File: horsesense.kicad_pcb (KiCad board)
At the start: 4 copper layers, 30 x 60 mm, 65 parts, among them J1 USB4105-GF-A-120, J2 S2B-PH-SM4-TB, J3 73412-0110, J4 Conn_01x04, SW1 EVQ-P7A01P, SW2 EVQ-P7A01P, U1 MAX86141ENP+T, U2 TXB0304RUT, U3 BQ25601, U4 XC6210B332MR, U5 XC6210B182MR, U6 LC76GPAMD, U7 AP22804AW5, U9 ESP32-S3-WROOM-1-N16R8

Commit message: Set MPN
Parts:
- D1, D2, D3: value CT DBLP31.12-5C8C-56-J6Q6 -> CT DBLP31.12-6C5D-56-J6U6-20-R18
- L1: footprint Inductor_SMD:L_2010_5025Metric -> Inductor_SMD:L_0805_2012Metric
- R7: value R -> 0
- U2: value TXB0304RUT -> TXB0304RUTR
- U7: value AP22804AW5 -> AP22804AW5-7
- moved C14 2.81 mm to (145.1, 138.1), turned to 90 degrees
- moved L1 1.37 mm to (149.1, 137.7)
- moved C11 0.98 mm to (146.8, 142.6)
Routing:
- net Vsys: track 54.7 -> 57.8 mm, vias 6 -> 4
- net GND: track 73.1 -> 72.1 mm, vias 44 -> 43

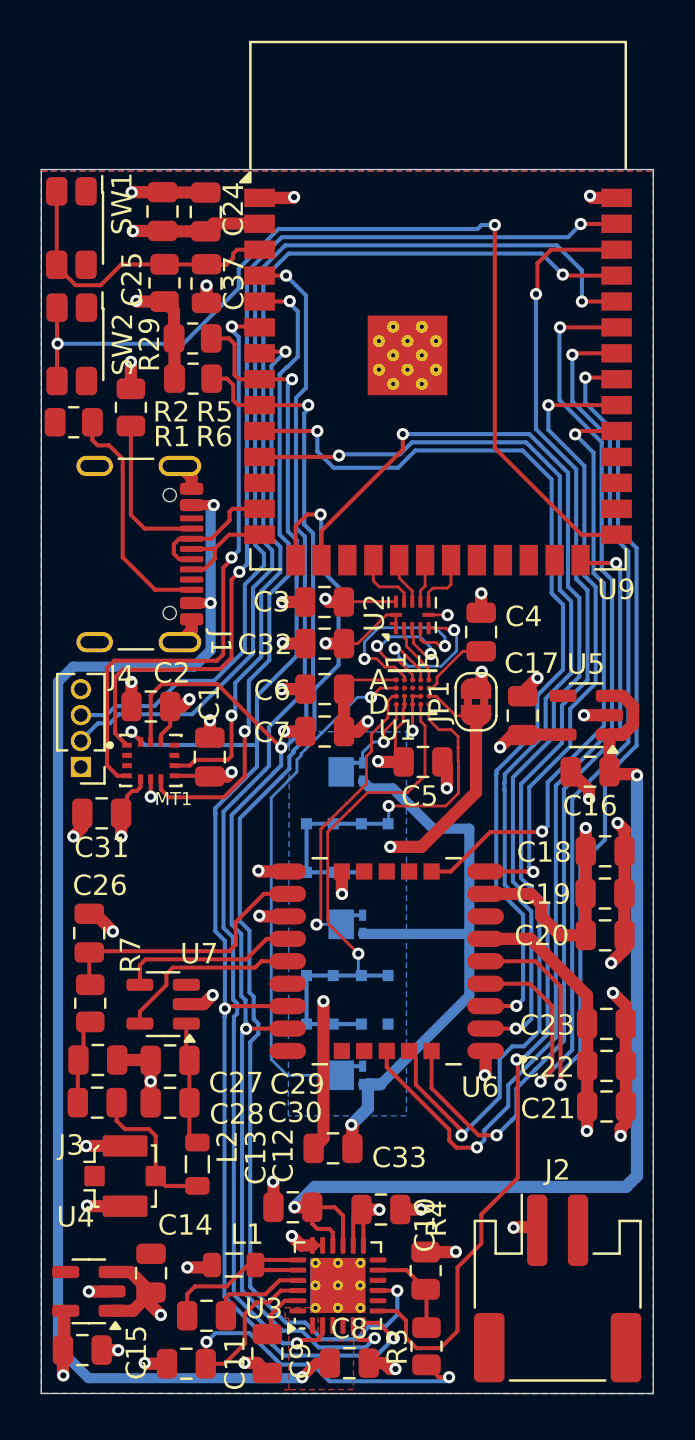
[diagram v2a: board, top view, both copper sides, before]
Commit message: Add Flash device
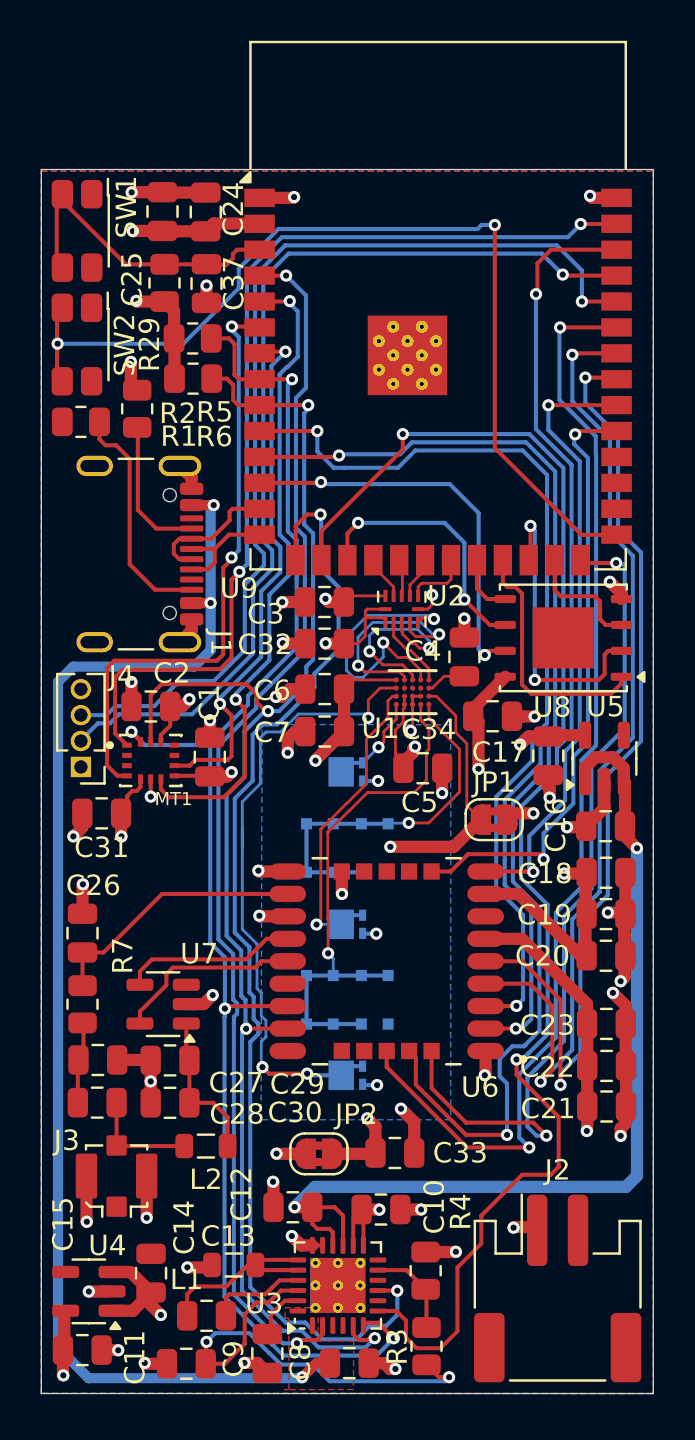
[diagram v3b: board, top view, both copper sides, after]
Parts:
- added C34: 100n, Capacitor_SMD:C_0805_2012Metric, F.Cu at (161.8, 110.8)
- added JP2: SolderJumper_2_Bridged, Jumper:SolderJumper-2_P1.3mm_Bridged2Bar_RoundedPad1.0x1.5mm, F.Cu at (153.3, 132.3)
- added U8: MX25L3233FM2, Package_DFN_QFN:W-PDFN-8-1EP_6x5mm_P1.27mm_EP3x3mm, F.Cu at (165.3, 107.0)
- moved JP1 5.85 mm to (161.9, 115.9), turned to 0 degrees
- moved C33 3.04 mm to (157.0, 132.2), turned to 0 degrees
- moved C16 2.78 mm to (167.3, 116.2)
- moved C17 2.33 mm to (164.5, 112.8), turned to -90 degrees
- moved U5 2.30 mm to (167.3, 112.9), turned to 90 degrees
- moved C4 1.47 mm to (160.4, 107.9)
- moved C18 1.05 mm to (167.4, 118.5)
- moved C19 1.01 mm to (167.4, 120.5)
- moved C20 1.00 mm to (167.4, 122.6)
- moved L2 0.98 mm to (147.8, 131.9), turned to 0 degrees
- moved U2 0.59 mm to (157.4, 105.6)
- moved J3 0.42 mm to (143.4, 133.4), turned to 180 degrees
- moved R7 0.38 mm to (141.7, 124.9)
- moved R1 0.35 mm to (141.6, 96.4)
- moved C26 0.33 mm to (141.7, 121.5)
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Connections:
- C33 pad 1: +3.3V -> +3.3V_LED
- D1 pad 2: +3.3V -> +3.3V_LED
- D2 pad 2: +3.3V -> +3.3V_LED
- D3 pad 2: +3.3V -> +3.3V_LED
- U9 pad 12: unconnected-(U9-IO8-Pad12) -> FLASH_SID3
- U9 pad 17: unconnected-(U9-IO9-Pad17) -> FLASH_SCLK
- U9 pad 22: unconnected-(U9-IO14-Pad22) -> FLASH_SID0
- U9 pad 23: unconnected-(U9-IO21-Pad23) -> FLASH_CS
- U9 pad 24: unconnected-(U9-IO47-Pad24) -> FLASH_SID1
- U9 pad 25: unconnected-(U9-IO48-Pad25) -> FLASH_SID2
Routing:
- net +3.3V: track 88.5 -> 64.5 mm, vias 11 -> 12
- net FLASH_SID3: track 0.00 -> 19.6 mm, vias 0 -> 2
- net FLASH_SID1: track 0.00 -> 14.9 mm, vias 0 -> 2
- net FLASH_SCLK: track 0.00 -> 13.0 mm, vias 0 -> 2
- net FLASH_CS: track 0.00 -> 12.5 mm
- net +3.3V_LED: track 0.00 -> 6.16 mm, vias 0 -> 4
- net FLASH_SID2: track 0.00 -> 5.98 mm
- net Net-(D3-K): track 26.6 -> 31.7 mm, vias 1 -> 3
- net MAX_MOSI_1_8: track 8.41 -> 13.3 mm
- net PD_GND: track 19.3 -> 14.7 mm
- net GND: track 72.1 -> 76.4 mm, vias 43 -> 44
- net Vsys: track 57.8 -> 54.5 mm
- net FLASH_SID0: track 0.00 -> 2.99 mm
- net GPS_FIX: track 38.5 -> 41.3 mm
- net SDA: track 75.0 -> 72.7 mm
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- added copper zone on In2.Cu, net +3.3V_LED

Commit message: Add mire and sizing marks
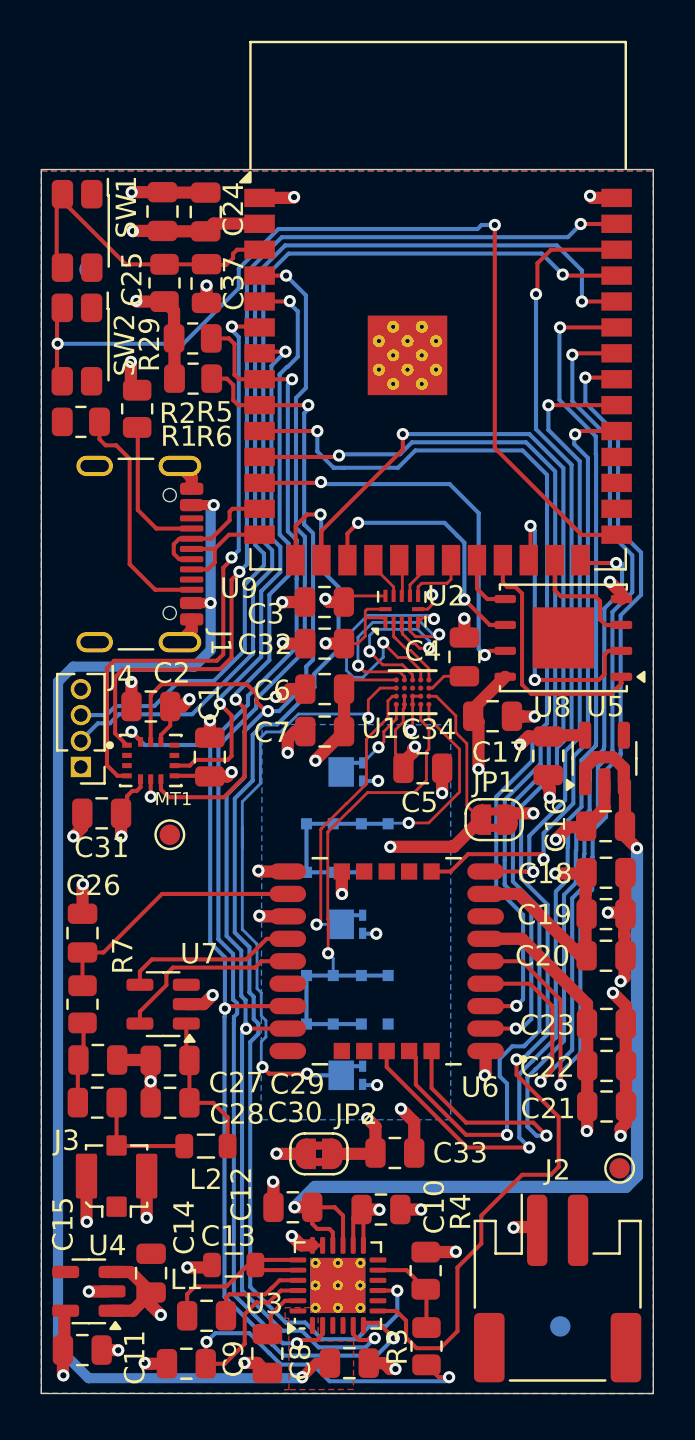
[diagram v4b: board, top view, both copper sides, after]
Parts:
- added TP1: Mire1_Top, TestPoint:TestPoint_Pad_D1.0mm, F.Cu at (146.0, 116.6)
- added TP2: Mire2_Top, TestPoint:TestPoint_Pad_D1.0mm, F.Cu at (168.0, 133.0)
- added TP3: Mire1_Bot, TestPoint:TestPoint_Pad_D1.0mm, B.Cu at (165.1, 140.7)
- added TP4: Mire2_Bot, TestPoint:TestPoint_Pad_D1.0mm, B.Cu at (142.1, 88.9)
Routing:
- net GND: track 76.4 -> 77.2 mm

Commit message: Ass logo
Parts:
- added SYM1: https://github.com/Philippe12/HorseSense, Symbol:OSHW-Symbol_13.4x12mm_SilkScreen, B.Cu at (158.7, 92.8)
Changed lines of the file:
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@@
+		(embedded_fonts no)
+	)
+	(footprint "Symbol:OSHW-Symbol_13.4x12mm_SilkScreen"
+		(layer "B.Cu")
+		(at 158.71 92.81 -90)
+		(descr "Open Source Hardware Symbol")
+		(tags "Logo Symbol OSHW")
+		(property "Reference" "SYM1"
+			(at 0 0 90)
+			(layer "B.SilkS")
+			(hide yes)
+			(effects
+				(font
+					(size 1 1)
+					(thickness 0.15)
+				)
+				(justify mirror)
+			)
+		)
+		(property "Value" "https://github.com/Philippe12/HorseSense"
+			(at 9.82 -8.79 90)
+			(layer "B.SilkS")
+			(effects
+				(font
+					(size 1 1)
+					(thickness 0.15)
+				)
+				(justify mirror)
+			)
+		)
+		(property "Datasheet" "~"
+			(at 0 0 90)
+			(unlocked yes)
+			(layer "B.Fab")
+			(hide yes)
+			(effects
+				(font
+					(size 1.27 1.27)
+					(thickness 0.15)
+				)
+				(justify mirror)
+			)
+		)
+		(property "Description" "Open Hardware logo, large"
+			(at 0 0 90)
+			(unlocked yes)
+			(layer "B.Fab")
+			(hide yes)
+			(effects
+				(font
+					(size 1.27 1.27)
+					(thickness 0.15)
+				)
+				(justify mirror)
+			)
+		)
+		(property "Sim.Enable" "0"
+			(at 0 0 90)
+			(unlocked yes)
+			(layer "B.Fab")
+			(hide yes)
+			(effects
+				(font
+					(size 1 1)
+					(thickness 0.15)
+				)
+				(justify mirror)
+			)
+		)
+		(sheetname "/")
+		(sheetfile "horsesense.kicad_sch")
+		(attr exclude_from_pos_files exclude_from_bom allow_missing_courtyard)
+		(fp_poly
+			(pts
+				(xy 1.119803 5.09936) (xy 1.288676 4.203573) (xy 1.911796 3.946702) (xy 2.534916 3.689832) (xy 3.282453 4.198151)
+				(xy 3.491802 4.339684) (xy 3.681043 4.466055) (xy 3.841343 4.571493) (xy 3.963874 4.65023) (xy 4.039802 4.696495)
+				(xy 4.06048 4.706471) (xy 4.097731 4.680814) (xy 4.177332 4.609885) (xy 4.290361 4.502743) (xy 4.427895 4.36845)
+				(xy 4.581012 4.216066) (xy 4.740789 4.054653) (xy 4.898305 3.89327) (xy 5.044637 3.740978) (xy 5.170863 3.606838)
+				(xy 5.26806 3.499911) (xy 5.327307 3.429258) (xy 5.341471 3.405612) (xy 5.321087 3.362021) (xy 5.263941 3.266519)
+				(xy 5.176041 3.12845) (xy 5.063396 2.957155) (xy 4.932013 2.761975) (xy 4.855882 2.650648) (xy 4.717118 2.447367)
+				(xy 4.593811 2.263927) (xy 4.491945 2.109458) (xy 4.417501 1.993091) (xy 4.376461 1.923958) (xy 4.370294 1.90943)
+				(xy 4.384274 1.86814) (xy 4.422382 1.771908) (xy 4.478867 1.634266) (xy 4.54798 1.468742) (xy 4.62397 1.288868)
+				(xy 4.701089 1.108172) (xy 4.773585 0.940186) (xy 4.835709 0.79844) (xy 4.881712 0.696463) (xy 4.905843 0.647786)
+				(xy 4.907267 0.64587) (xy 4.945158 0.636575) (xy 5.046069 0.61584) (xy 5.19954 0.585702) (xy 5.395112 0.548199)
+				(xy 5.622325 0.505371) (xy 5.754891 0.480674) (xy 5.997679 0.434447) (xy 6.216974 0.39046) (xy 6.401681 0.351119)
+				(xy 6.540705 0.318831) (xy 6.622952 0.296003) (xy 6.639485 0.28876) (xy 6.655678 0.239739) (xy 6.668744 0.129023)
+				(xy 6.678691 -0.030438) (xy 6.685528 -0.2257) (xy 6.689264 -0.443814) (xy 6.689907 -0.671835) (xy 6.687468 -0.896815)
+				(xy 6.681953 -1.105809) (xy 6.673374 -1.285868) (xy 6.661737 -1.424047) (xy 6.647052 -1.507398)
+				(xy 6.638245 -1.52475) (xy 6.585599 -1.545548) (xy 6.474043 -1.575282) (xy 6.318335 -1.610459) (xy 6.133229 -1.647586)
+				(xy 6.068613 -1.659597) (xy 5.757071 -1.716662) (xy 5.510976 -1.762618) (xy 5.322195 -1.799293)
+				(xy 5.182598 -1.828513) (xy 5.084052 -1.852104) (xy 5.018426 -1.871892) (xy 4.977589 -1.889706)
+				(xy 4.953409 -1.90737) (xy 4.950026 -1.910861) (xy 4.916255 -1.9671) (xy 4.864737 -2.076547) (xy 4.800617 -2.2258)
+				(xy 4.729039 -2.401459) (xy 4.655146 -2.590121) (xy 4.584083 -2.778385) (xy 4.520993 -2.952848)
+				(xy 4.471021 -3.100108) (xy 4.439312 -3.206764) (xy 4.431008 -3.259413) (xy 4.4317 -3.261257) (xy 4.459836 -3.304292)
+				(xy 4.523665 -3.398978) (xy 4.61648 -3.53546) (xy 4.731573 -3.703882) (xy 4.862237 -3.89439) (xy 4.899448 -3.948529)
+				(xy 5.032129 -4.144804) (xy 5.148883 -4.323886) (xy 5.243349 -4.475492) (xy 5.309168 -4.589338)
+				(xy 5.339978 -4.655141) (xy 5.341471 -4.663225) (xy 5.315584 -4.705715) (xy 5.244054 -4.789891)
+				(xy 5.136076 -4.906705) (xy 5.000846 -5.04711) (xy 4.847558 -5.202061) (xy 4.685409 -5.362509) (xy 4.523593 -5.519409)
+				(xy 4.371306 -5.663713) (xy 4.237743 -5.786376) (xy 4.1321 -5.87835) (xy 4.063572 -5.930589) (xy 4.044614 -5.939118)
+				(xy 4.000487 -5.919029) (xy 3.910142 -5.864849) (xy 3.788295 -5.785704) (xy 3.694546 -5.722001)
+				(xy 3.524678 -5.60511) (xy 3.323512 -5.467476) (xy 3.121733 -5.330063) (xy 3.01325 -5.256519) (xy 2.646058 -5.008155)
+				(xy 2.337826 -5.174813) (xy 2.197404 -5.247822) (xy 2.077996 -5.304571) (xy 1.997202 -5.336937)
+				(xy 1.976636 -5.341441) (xy 1.951906 -5.308189) (xy 1.903118 -5.214224) (xy 1.833913 -5.068213)
+				(xy 1.747935 -4.878824) (xy 1.648824 -4.654724) (xy 1.540224 -4.404581) (xy 1.425775 -4.137063)
+				(xy 1.30912 -3.860836) (xy 1.193901 -3.584568) (xy 1.08376 -3.316927) (xy 0.982339 -3.06658) (xy 0.89328 -2.842195)
+				(xy 0.820225 -2.652439) (xy 0.766816 -2.50598) (xy 0.736695 -2.411485) (xy 0.731851 -2.379031) (xy 0.770245 -2.337636)
+				(xy 0.854308 -2.270438) (xy 0.966467 -2.1914) (xy 0.975881 -2.185147) (xy 1.265768 -1.953103) (xy 1.499512 -1.682386)
+				(xy 1.675087 -1.381653) (xy 1.790469 -1.059561) (xy 1.84363 -0.724765) (xy 1.832547 -0.385922) (xy 1.755192 -0.051688)
+				(xy 1.60954 0.269281) (xy 1.566688 0.339505) (xy 1.343802 0.623073) (xy 1.080491 0.850782) (xy 0.785865 1.021449)
+				(xy 0.469041 1.133888) (xy 0.13913 1.186917) (xy -0.194754 1.179349) (xy -0.523497 1.110002) (xy -0.837986 0.977691)
+				(xy -1.129107 0.781232) (xy -1.21916 0.701494) (xy -1.448347 0.451892) (xy -1.615354 0.189132) (xy -1.729915 -0.105399)
+				(xy -1.793719 -0.397075) (xy -1.80947 -0.725012) (xy -1.756949 -1.054577) (xy -1.64149 -1.37463)
+				(xy -1.468429 -1.674032) (xy -1.243101 -1.941643) (xy -0.97084 -2.166325) (xy -0.935058 -2.190008)
+				(xy -0.821698 -2.267568) (xy -0.735522 -2.334768) (xy -0.694323 -2.377675) (xy -0.693724 -2.379031)
+				(xy -0.702569 -2.425446) (xy -0.737631 -2.530786) (xy -0.795267 -2.686388) (xy -0.871834 -2.883584)
+				(xy -0.963686 -3.11371) (xy -1.067183 -3.368101) (xy -1.178679 -3.63809) (xy -1.294532 -3.915012)
+				(xy -1.411097 -4.190201) (xy -1.524733 -4.454993) (xy -1.631794 -4.700721) (xy -1.728638 -4.918721)
+				(xy -1.811621 -5.100326) (xy -1.877099 -5.236871) (xy -1.921431 -5.31969) (xy -1.939283 -5.341441)
+				(xy -1.993834 -5.324504) (xy -2.095905 -5.279077) (xy -2.227895 -5.21328) (xy -2.300474 -5.174813)
+				(xy -2.608705 -5.008155) (xy -2.975897 -5.256519) (xy -3.16334 -5.383754) (xy -3.368557 -5.523773)
+				(xy -3.560867 -5.655612) (xy -3.657193 -5.722001) (xy -3.792673 -5.812976) (xy -3.907393 -5.885071)
+				(xy -3.986388 -5.929154) (xy -4.012046 -5.938473) (xy -4.049391 -5.913334) (xy -4.132042 -5.843154)
+				(xy -4.251985 -5.73522) (xy -4.401209 -5.596818) (xy -4.571699 -5.435235) (xy -4.679526 -5.331488)
+				(xy -4.868172 -5.146135) (xy -5.031205 -4.980351) (xy -5.162032 -4.841227) (xy -5.254065 -4.735856)
+				(xy -5.300713 -4.671329) (xy -5.305188 -4.658234) (xy -5.28442 -4.608425) (xy -5.227031 -4.507713)
+				(xy -5.139387 -4.366295) (xy -5.027854 -4.194367) (xy -4.898797 -4.002124) (xy -4.862096 -3.948529)
+				(xy -4.728368 -3.753733) (xy -4.608393 -3.578353) (xy -4.508879 -3.432243) (xy -4.436533 -3.325258)
+				(xy -4.398064 -3.267255) (xy -4.394347 -3.261257) (xy -4.399905 -3.215032) (xy -4.429407 -3.113398)
+				(xy -4.477709 -2.969758) (xy -4.539667 -2.797514) (xy -4.610137 -2.610066) (xy -4.683975 -2.420818)
+				(xy -4.756037 -2.243171) (xy -4.821178 -2.090527) (xy -4.874255 -1.976288) (xy -4.910123 -1.913856)
+				(xy -4.912673 -1.910861) (xy -4.934606 -1.893019) (xy -4.971652 -1.875374) (xy -5.031941 -1.856101)
+				(xy -5.123604 -1.833374) (xy -5.254774 -1.805364) (xy -5.433582 -1.770247) (xy -5.668158 -1.726195)
+				(xy -5.966635 -1.671382) (xy -6.03126 -1.659597) (xy -6.222794 -1.622591) (xy -6.389769 -1.586389)
+				(xy -6.517432 -1.554485) (xy -6.591024 -1.530372) (xy -6.600892 -1.52475) (xy -6.617153 -1.47491)
+				(xy -6.63037 -1.363532) (xy -6.640536 -1.203563) (xy -6.64764 -1.00795) (xy -6.651674 -0.78964)
+				(xy -6.65263 -0.561579) (xy -6.650498 -0.336714) (xy -6.645269 -0.127991) (xy -6.636935 0.051642)
+				(xy -6.625487 0.189238) (xy -6.610916 0.271852) (xy -6.602132 0.28876) (xy -6.55323 0.305816) (xy -6.441873 0.333564)
+				(xy -6.279156 0.369597) (xy -6.076174 0.411507) (xy -5.844021 0.456889) (xy -5.717538 0.480674)
+				(xy -5.477555 0.525535) (xy -5.263549 0.566175) (xy -5.085978 0.600554) (xy -4.955302 0.626635)
+				(xy -4.881982 0.642379) (xy -4.869915 0.64587) (xy -4.849519 0.685221) (xy -4.806406 0.780007) (xy -4.746321 0.916685)
+				(xy -4.675013 1.081714) (xy -4.598227 1.261553) (xy -4.52171 1.44266) (xy -4.45121 1.611493) (xy -4.392473 1.754512)
+				(xy -4.351246 1.858174) (xy -4.333276 1.908939) (xy -4.332941 1.911158) (xy -4.353313 1.951204)
+				(xy -4.410427 2.043361) (xy -4.498279 2.178467) (xy -4.610867 2.347365) (xy -4.742189 2.540895)
+				(xy -4.818529 2.652059) (xy -4.957636 2.855884) (xy -5.081188 3.040937) (xy -5.183158 3.197854)
+				(xy -5.257517 3.317276) (xy -5.298237 3.38984) (xy -5.304118 3.406107) (xy -5.278837 3.44397) (xy -5.208948 3.524814)
+				(xy -5.103377 3.639581) (xy -4.971052 3.779215) (xy -4.820901 3.934658) (xy -4.661852 4.096854)
+				(xy -4.502833 4.256746) (xy -4.352771 4.405276) (xy -4.220594 4.533387) (xy -4.11523 4.632023) (xy -4.045607 4.692127)
+				(xy -4.022315 4.706471) (xy -3.98439 4.686301) (xy -3.893683 4.629637) (xy -3.759011 4.542247) (xy -3.589195 4.4299)
+				(xy -3.393054 4.298362) (xy -3.2451 4.198151) (xy -2.497564 3.689832) (xy -1.874444 3.946702) (xy -1.251324 4.203573)
+				(xy -0.913576 5.995147) (xy 0.950929 5.995147) (xy 1.119803 5.09936)
+			)
+			(stroke
+				(width 0.01)
+				(type solid)
+			)
+			(fill yes)
+			(layer "B.SilkS")
+		)
 		(embedded_fonts no)
 	)
